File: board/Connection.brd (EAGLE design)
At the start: 125.4 x 71.1 mm, 35 parts, among them CN3 CN3, CN4 CN4, U2 SN65HVD230, U5 ADA4528-1ARMZ-R7, X1 MKDSN1,5/4-5,08, X2 MKDSN1,5/2-5,08

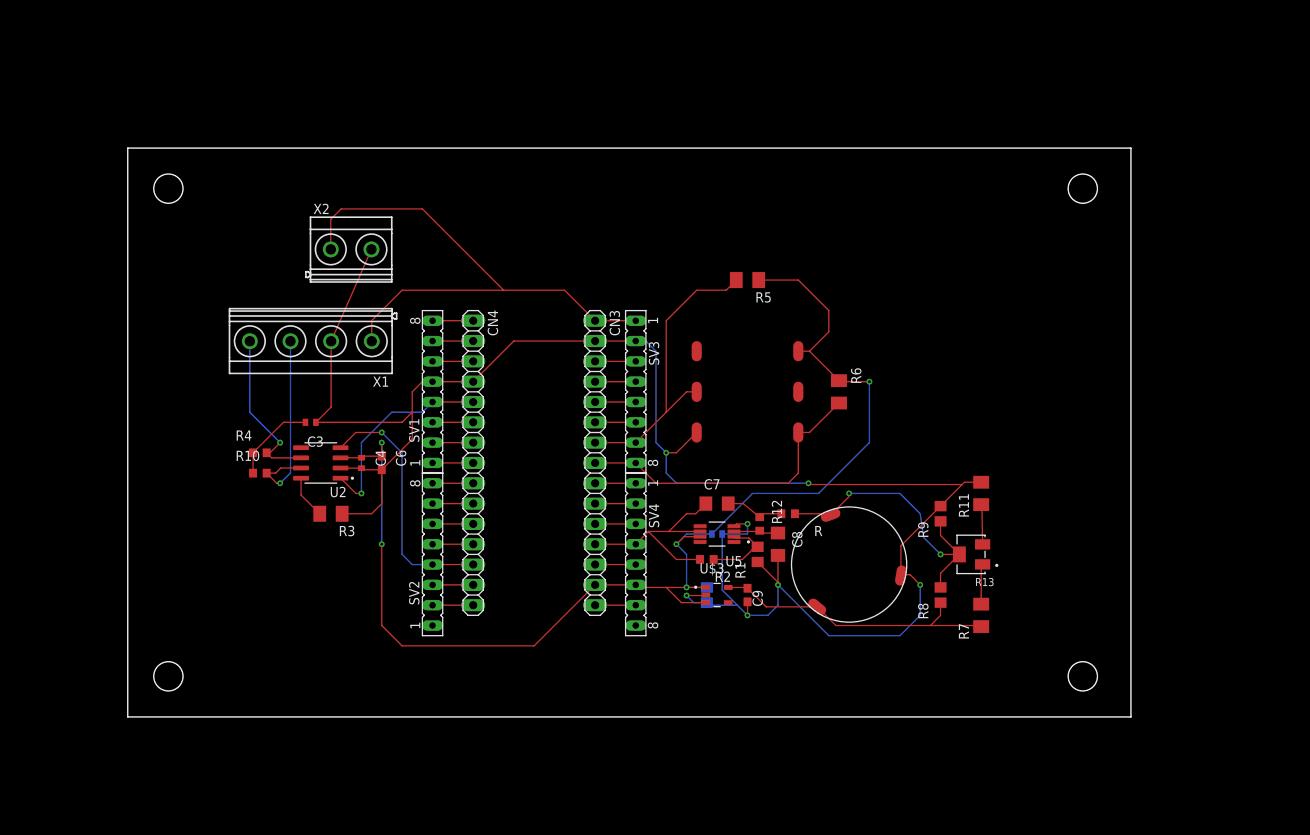
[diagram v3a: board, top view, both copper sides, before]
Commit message: Modifications: 1. Flipped components to top layer 2. rearrange the spaces 3. Bolded pwr wires 4. Added copper 5. Sensor inlets toward edge 6. Terminals locked
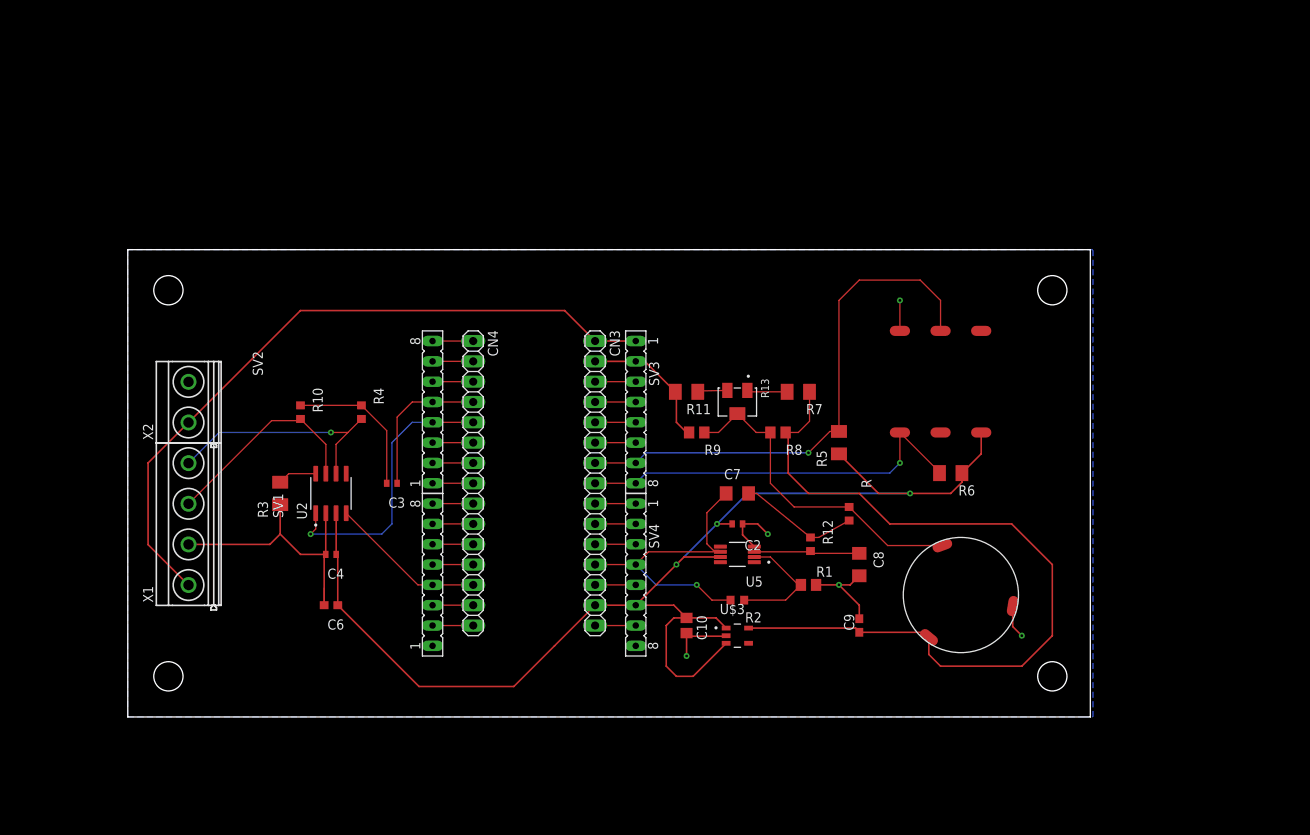
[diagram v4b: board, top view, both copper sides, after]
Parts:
- moved R11 39.0 mm to (69.8, 40.6), turned to 180 degrees
- moved R7 36.1 mm to (83.8, 40.6), turned to 180 degrees
- moved R13 34.9 mm to (76.2, 39.4), turned to 270 degrees
- moved R9 32.1 mm to (71.1, 35.6), turned to 180 degrees
- moved R8 28.7 mm to (81.3, 35.6), turned to 180 degrees
- moved X2 27.9 mm to (7.62, 39.4), turned to 90 degrees
- moved X1 27.5 mm to (7.62, 24.1), turned to 90 degrees
- moved U$4 25.0 mm to (106.7, 35.6), turned to 180 degrees
- moved R5 23.3 mm to (88.9, 34.3), turned to 90 degrees
- moved C6 18.9 mm to (25.4, 14.0), turned to 180 degrees
- moved R6 17.3 mm to (102.9, 30.5), turned to 180 degrees
- moved C9 14.5 mm to (91.4, 11.4), turned to 90 degrees
- moved U$1 14.5 mm to (104.1, 15.2)
- moved R4 13.7 mm to (29.2, 38.1), turned to 270 degrees
- moved C3 12.7 mm to (33.0, 29.2)
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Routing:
- net GND: track 242.7 -> 106.7 mm, vias 7 -> 5
- net 3V: track 37.0 -> 102.1 mm
- net SCL: track 37.6 -> 67.1 mm, vias 0 -> 1
- net +12V: track 68.9 -> 87.8 mm
- net RX: track 31.6 -> 19.6 mm, vias 1 -> 0
- net ADC: track 27.8 -> 39.4 mm, vias 0 -> 1
- net SDA: track 38.7 -> 50.1 mm, vias 0 -> 1
- net TX: track 25.8 -> 34.9 mm
- net CANL: track 21.0 -> 29.7 mm
- net C1: track 10.7 -> 18.7 mm
- net IN+: track 5.90 -> 13.5 mm
- net F1: track 7.62 -> 15.1 mm
- net IN-: track 9.55 -> 15.1 mm
- net OUTPUT: track 36.7 -> 41.3 mm, vias 2 -> 0
- net 3V3: track 156.1 -> 160.6 mm, vias 5 -> 3
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- added copper zone on layer 16, net GND
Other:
- board size 125.4 x 71.1 mm -> 120.3 x 58.4 mm

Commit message: Polished the design
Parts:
- moved C3 18.2 mm to (16.5, 36.8), turned to 0 degrees
- moved R4 9.25 mm to (20.3, 40.6), turned to 90 degrees
- moved C2 6.98 mm to (76.2, 17.1)
- moved R10 2.84 mm to (20.3, 35.6)
- moved C7 2.54 mm to (76.2, 25.4)
- moved C6 2.54 mm to (25.4, 16.5)
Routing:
- net 3V3: track 160.6 -> 201.2 mm, vias 3 -> 0
- net GND: track 106.7 -> 90.7 mm, vias 5 -> 7
- net C1: track 18.7 -> 6.71 mm
- net 3V: track 102.1 -> 97.4 mm
- net CANL: track 29.7 -> 32.8 mm, vias 1 -> 0
- net CANH: track 26.7 -> 23.7 mm
- net ADC: track 39.4 -> 36.9 mm
- net RX: track 19.6 -> 21.1 mm
- net F1: track 15.1 -> 14.2 mm

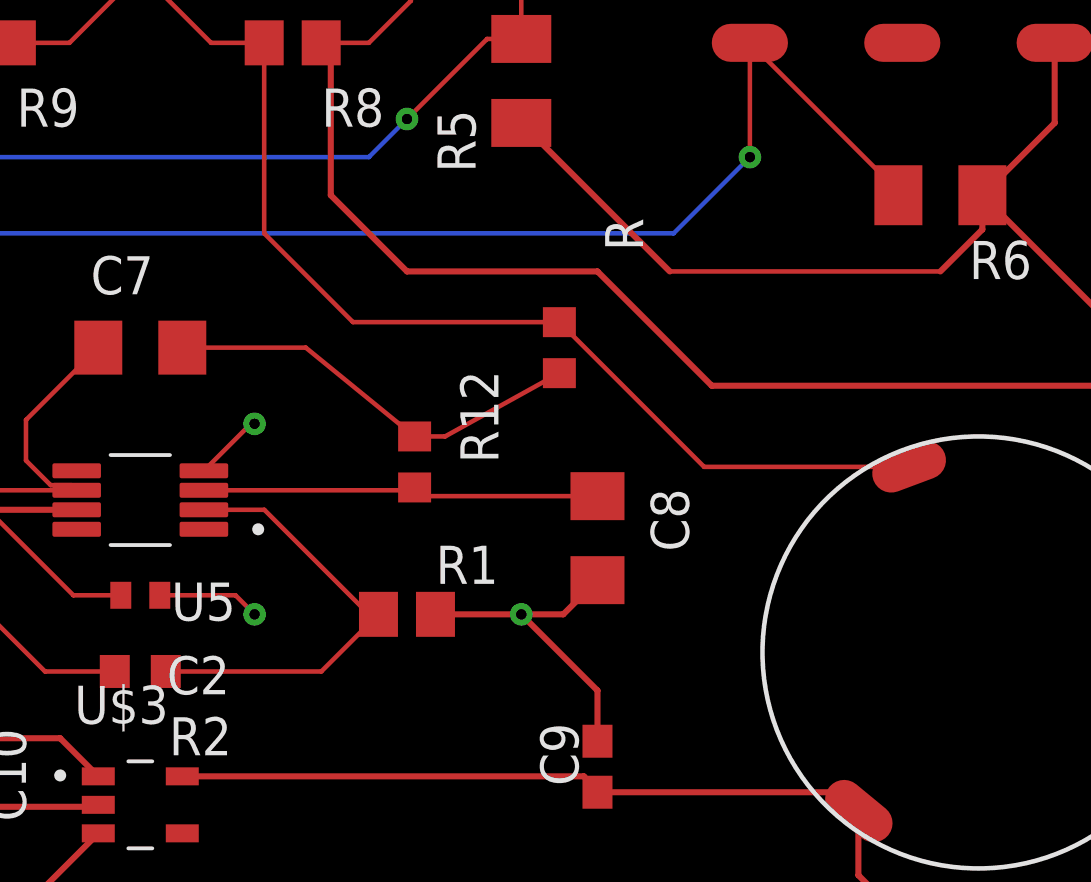
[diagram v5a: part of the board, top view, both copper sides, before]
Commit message: Updated the design according to the real connection.
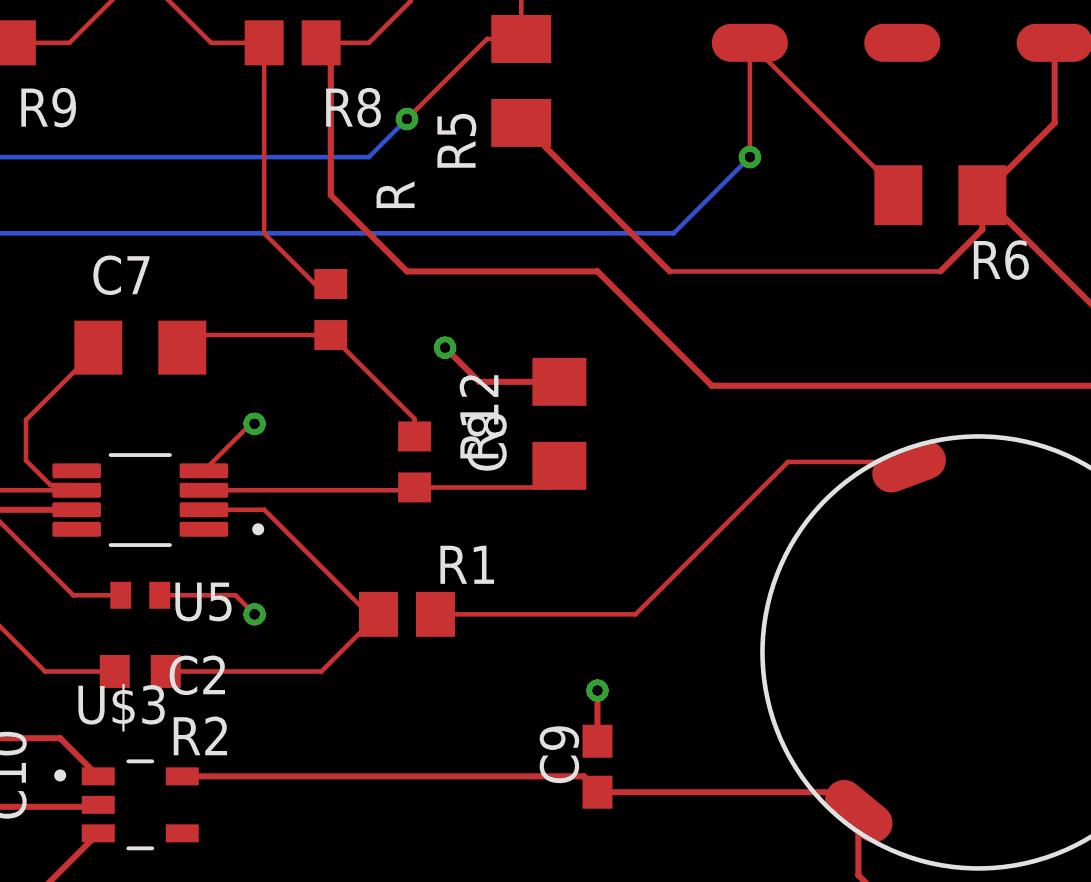
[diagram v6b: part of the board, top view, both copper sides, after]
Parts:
- moved R 7.73 mm to (82.5, 26.7)
- moved C8 4.02 mm to (90.2, 22.9), turned to 90 degrees
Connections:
- new net OUTIN-: R1.1, U$1.P$1
- net GND: no longer R1.1
- net OUTPUT: no longer U$1.P$1
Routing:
- net OUTPUT: track 41.3 -> 19.5 mm
- net OUTIN-: track 0.00 -> 18.0 mm
- net GND: track 90.7 -> 85.5 mm, vias 7 -> 8
- net F1: track 14.2 -> 9.66 mm
- net IN+: track 13.5 -> 12.3 mm
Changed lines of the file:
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@@
 <attribute name="VALUE" x="27.051" y="19.558" size="1.27" layer="27" ratio="10" rot="R180"/>
 </element>
-<element name="R" library="rcl" library_urn="urn:adsk.eagle:library:334" package="R0603" package3d_urn="urn:adsk.eagle:package:23555/3" value="6k49" x="90.17" y="25.4" smashed="yes" rot="R270">
-<attribute name="NAME" x="91.694" y="29.718" size="1.27" layer="25" ratio="10" rot="R270"/>
-<attribute name="POPULARITY" value="77" x="90.17" y="25.4" size="1.778" layer="27" rot="R270" display="off"/>
-<attribute name="SPICEPREFIX" value="R" x="90.17" y="25.4" size="1.778" layer="27" rot="R270" display="off"/>
-<attribute name="VALUE" x="89.535" y="27.6606" size="1.27" layer="27" ratio="10" rot="R270"/>
+<element name="R" library="rcl" library_urn="urn:adsk.eagle:library:334" package="R0603" package3d_urn="urn:adsk.eagle:package:23555/3" value="6k49" x="82.55" y="26.67" smashed="yes" rot="R270">
+<attribute name="NAME" x="84.074" y="30.988" size="1.27" layer="25" ratio="10" rot="R270"/>
+<attribute name="POPULARITY" value="77" x="82.55" y="26.67" size="1.778" layer="27" rot="R270" display="off"/>
+<attribute name="SPICEPREFIX" value="R" x="82.55" y="26.67" size="1.778" layer="27" rot="R270" display="off"/>
+<attribute name="VALUE" x="81.915" y="28.9306" size="1.27" layer="27" ratio="10" rot="R270"/>
 </element>
 <element name="R12" library="rcl" library_urn="urn:adsk.eagle:library:334" package="R0603" package3d_urn="urn:adsk.eagle:package:23555/3" value="49k9" x="85.344" y="21.59" smashed="yes" rot="R270">
@@
 <attribute name="VALUE" x="74.549" y="22.352" size="1.27" layer="27" ratio="10"/>
 </element>
-<element name="C8" library="rcl" library_urn="urn:adsk.eagle:library:334" package="C1206" package3d_urn="urn:adsk.eagle:package:23618/2" value="4.7uF" x="91.44" y="19.05" smashed="yes" rot="R270">
-<attribute name="NAME" x="93.218" y="20.701" size="1.27" layer="25" ratio="10" rot="R270"/>
-<attribute name="POPULARITY" value="24" x="91.44" y="19.05" size="1.778" layer="27" rot="R270" display="off"/>
-<attribute name="SPICEPREFIX" value="C" x="91.44" y="19.05" size="1.778" layer="27" rot="R270" display="off"/>
-<attribute name="VALUE" x="88.392" y="20.701" size="1.27" layer="27" ratio="10" rot="R270"/>
+<element name="C8" library="rcl" library_urn="urn:adsk.eagle:library:334" package="C1206" package3d_urn="urn:adsk.eagle:package:23618/2" value="4.7uF" x="90.17" y="22.86" smashed="yes" rot="R90">
+<attribute name="NAME" x="88.392" y="21.209" size="1.27" layer="25" ratio="10" rot="R90"/>
+<attribute name="POPULARITY" value="24" x="90.17" y="22.86" size="1.778" layer="27" rot="R90" display="off"/>
+<attribute name="SPICEPREFIX" value="C" x="90.17" y="22.86" size="1.778" layer="27" rot="R90" display="off"/>
+<attribute name="VALUE" x="93.218" y="21.209" size="1.27" layer="27" ratio="10" rot="R90"/>
 </element>
 <element name="R13" library="3224W1203E" package="TRIM_3224W1203E" value="3224W1203E" x="76.2" y="39.37" smashed="yes" rot="R270" grouprefs="13">
@@
 <contactref element="C4" pad="2"/>
 <contactref element="C6" pad="2"/>
-<contactref element="R1" pad="1"/>
-<contactref element="C8" pad="2"/>
 <contactref element="R3" pad="1"/>
 <contactref element="C3" pad="1"/>
@@
 <wire x1="7.595" y1="21.5689" x2="17.7589" y2="21.5689" width="0.2032" layer="1"/>
 <wire x1="17.7589" y1="21.5689" x2="19.05" y2="22.86" width="0.2032" layer="1"/>
-<wire x1="91.486490625" y1="17.696490625" x2="91.44" y2="17.65" width="0.1524" layer="1"/>
 <via x="69.85" y="7.62" extent="1-16" drill="0.35"/>
-<via x="88.9" y="16.51" extent="1-16" drill="0.35"/>
+<via x="91.44" y="13.97" extent="1-16" drill="0.35"/>
 <wire x1="68.45" y1="40.64" x2="68.45" y2="43.18" width="0.2032" layer="1"/>
 <wire x1="68.45" y1="43.18" x2="67.18" y2="44.45" width="0.2032" layer="1"/>
@@
 <wire x1="96.52" y1="48.26" x2="96.52" y2="52.07" width="0.1524" layer="1"/>
 <via x="96.52" y="52.07" extent="1-16" drill="0.35"/>
-<wire x1="88.9" y1="16.51" x2="91.44" y2="13.97" width="0.2032" layer="1"/>
 <wire x1="91.44" y1="13.97" x2="91.44" y2="12.28" width="0.2032" layer="1"/>
 <wire x1="110.619459375" y1="13.86615" x2="110.619459375" y2="13.840540625" width="0.2032" layer="1"/>
@@
 <wire x1="70.235" y1="10.095" x2="74.865" y2="10.095" width="0.2032" layer="1"/>
 <wire x1="69.85" y1="10.48" x2="69.85" y2="7.62" width="0.2032" layer="1"/>
-<wire x1="86.04" y1="16.51" x2="88.9" y2="16.51" width="0.2032" layer="1"/>
-<wire x1="91.44" y1="17.65" x2="90.3" y2="16.51" width="0.2032" layer="1"/>
-<wire x1="90.3" y1="16.51" x2="88.9" y2="16.51" width="0.2032" layer="1"/>
 <wire x1="78.32" y1="21.295" x2="79.885" y2="22.86" width="0.1524" layer="1"/>
 <wire x1="79.885" y1="22.86" x2="80.01" y2="22.86" width="0.1524" layer="1"/>
@@
 <wire x1="14.59" y1="35.56" x2="13.97" y2="35.56" width="0.1524" layer="1"/>
 <via x="13.97" y="35.56" extent="1-16" drill="0.35"/>
+<contactref element="C8" pad="2"/>
+<via x="86.36" y="25.4" extent="1-16" drill="0.35"/>
+<wire x1="90.17" y1="24.26" x2="87.5" y2="24.26" width="0.2032" layer="1"/>
+<wire x1="87.5" y1="24.26" x2="86.36" y2="25.4" width="0.2032" layer="1"/>
 </signal>
 <signal name="TX">
@@
 <contactref element="R9" pad="1"/>
 <contactref element="R13" pad="2"/>
-<contactref element="U$1" pad="P$1"/>
 <contactref element="R" pad="1"/>
 <wire x1="76.2" y1="37.92" x2="73.84" y2="35.56" width="0.1524" layer="1" grouprefs="13"/>
@@
 <wire x1="80.33" y1="35.56" x2="78.56" y2="35.56" width="0.1524" layer="1" grouprefs="13"/>
 <wire x1="78.56" y1="35.56" x2="76.2" y2="37.92" width="0.1524" layer="1" grouprefs="13"/>
-<wire x1="83.29" y1="26.25" x2="80.33" y2="29.21" width="0.1524" layer="1"/>
+<wire x1="82.02" y1="27.52" x2="80.33" y2="29.21" width="0.1524" layer="1"/>
 <wire x1="80.33" y1="35.56" x2="80.33" y2="29.21" width="0.1524" layer="1"/>
-<wire x1="83.29" y1="26.25" x2="90.17" y2="26.25" width="0.1524" layer="1"/>
-<wire x1="90.17" y1="26.25" x2="94.99421875" y2="21.42578125" width="0.1524" layer="1"/>
-<wire x1="94.99421875" y1="21.42578125" x2="101.827228125" y2="21.42578125" width="0.1524" layer="1"/>
+<wire x1="82.02" y1="27.52" x2="82.55" y2="27.52" width="0.1524" layer="1"/>
 </signal>
 <signal name="N$18">
@@
 <wire x1="78.32" y1="20.645" x2="84.868" y2="20.645" width="0.1524" layer="1"/>
 <wire x1="84.868" y1="20.645" x2="85.344" y2="20.74" width="0.1524" layer="1"/>
-<wire x1="85.344" y1="20.74" x2="85.253" y2="20.45" width="0.1524" layer="1"/>
-<wire x1="85.253" y1="20.45" x2="91.44" y2="20.45" width="0.1524" layer="1"/>
+<wire x1="90.17" y1="21.46" x2="89.84415625" y2="20.74" width="0.1524" layer="1"/>
+<wire x1="85.344" y1="20.74" x2="89.84415625" y2="20.74" width="0.1524" layer="1"/>
 </signal>
 <signal name="3V">
@@
 <contactref element="R12" pad="1"/>
 <contactref element="R" pad="2"/>
-<wire x1="90.17" y1="24.55" x2="86.36" y2="22.44" width="0.1524" layer="1"/>
-<wire x1="85.344" y1="22.44" x2="86.36" y2="22.44" width="0.1524" layer="1"/>
-<wire x1="85.344" y1="22.44" x2="81.7166875" y2="25.4" width="0.1524" layer="1"/>
-<wire x1="77.6" y1="25.4" x2="81.7166875" y2="25.4" width="0.1524" layer="1"/>
+<wire x1="77.6" y1="25.4" x2="78.02" y2="25.82" width="0.1524" layer="1"/>
+<wire x1="78.02" y1="25.82" x2="82.55" y2="25.82" width="0.1524" layer="1"/>
+<wire x1="82.55" y1="25.82" x2="85.344" y2="23.026" width="0.1524" layer="1"/>
+<wire x1="85.344" y1="23.026" x2="85.344" y2="22.44" width="0.1524" layer="1"/>
 </signal>
 <signal name="+12V">
@@
 <wire x1="2.54" y1="31.7539" x2="2.54" y2="21.5439" width="0.2032" layer="1"/>
 </signal>
+<signal name="OUTIN-">
+<contactref element="R1" pad="1"/>
+<contactref element="U$1" pad="P$1"/>
+<wire x1="86.04" y1="16.51" x2="92.71" y2="16.51" width="0.1524" layer="1"/>
+<wire x1="92.71" y1="16.51" x2="97.79" y2="21.59" width="0.1524" layer="1"/>
+<wire x1="97.79" y1="21.59" x2="101.663009375" y2="21.59" width="0.1524" layer="1"/>
+<wire x1="101.663009375" y1="21.59" x2="101.827228125" y2="21.42578125" width="0.1524" layer="1"/>
+</signal>
 </signals>
